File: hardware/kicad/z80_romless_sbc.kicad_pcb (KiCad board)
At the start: 2 copper layers, 160 x 135 mm, 69 parts, among them J1 REGULATED 5V INPUT, Q1 2N3904 MCP RESET, U1 Z84C0020PEC, U10 SN74LVC245AN bus-to-Pico, U2 AS6C1008-55PCN, U3 ATF22V10B/C, U4 SN74AHCT244N, U7 SN74LVC244AN, U8 MCP23S17-E/SP, U9 SN74AHCT245N Pico-to-bus

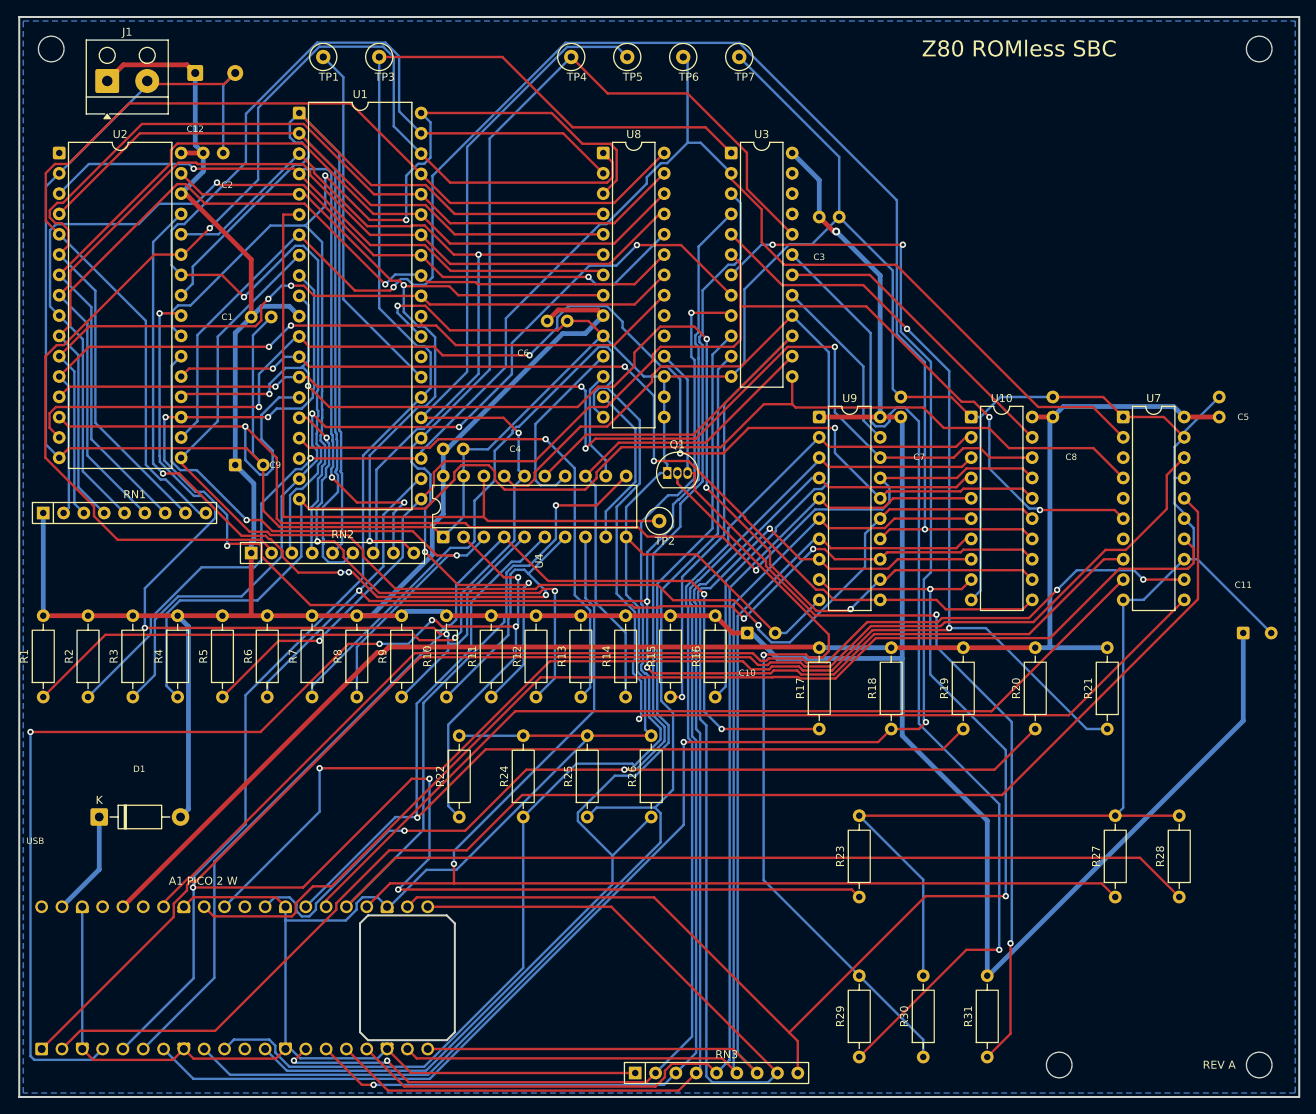
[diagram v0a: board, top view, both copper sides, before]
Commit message: feat: redesign PCB with four-layer stack
Reserve In1.Cu as a continuous ground plane, route signals on F.Cu/In2.Cu/B.Cu, and lock optimized via-free PICO_CLK and D4 paths for the 8 MHz qualification target. Regenerate and validate all KiCad and fabrication artifacts.

Co-authored-by: Copilot <223556219+Copilot@users.noreply.github.com>
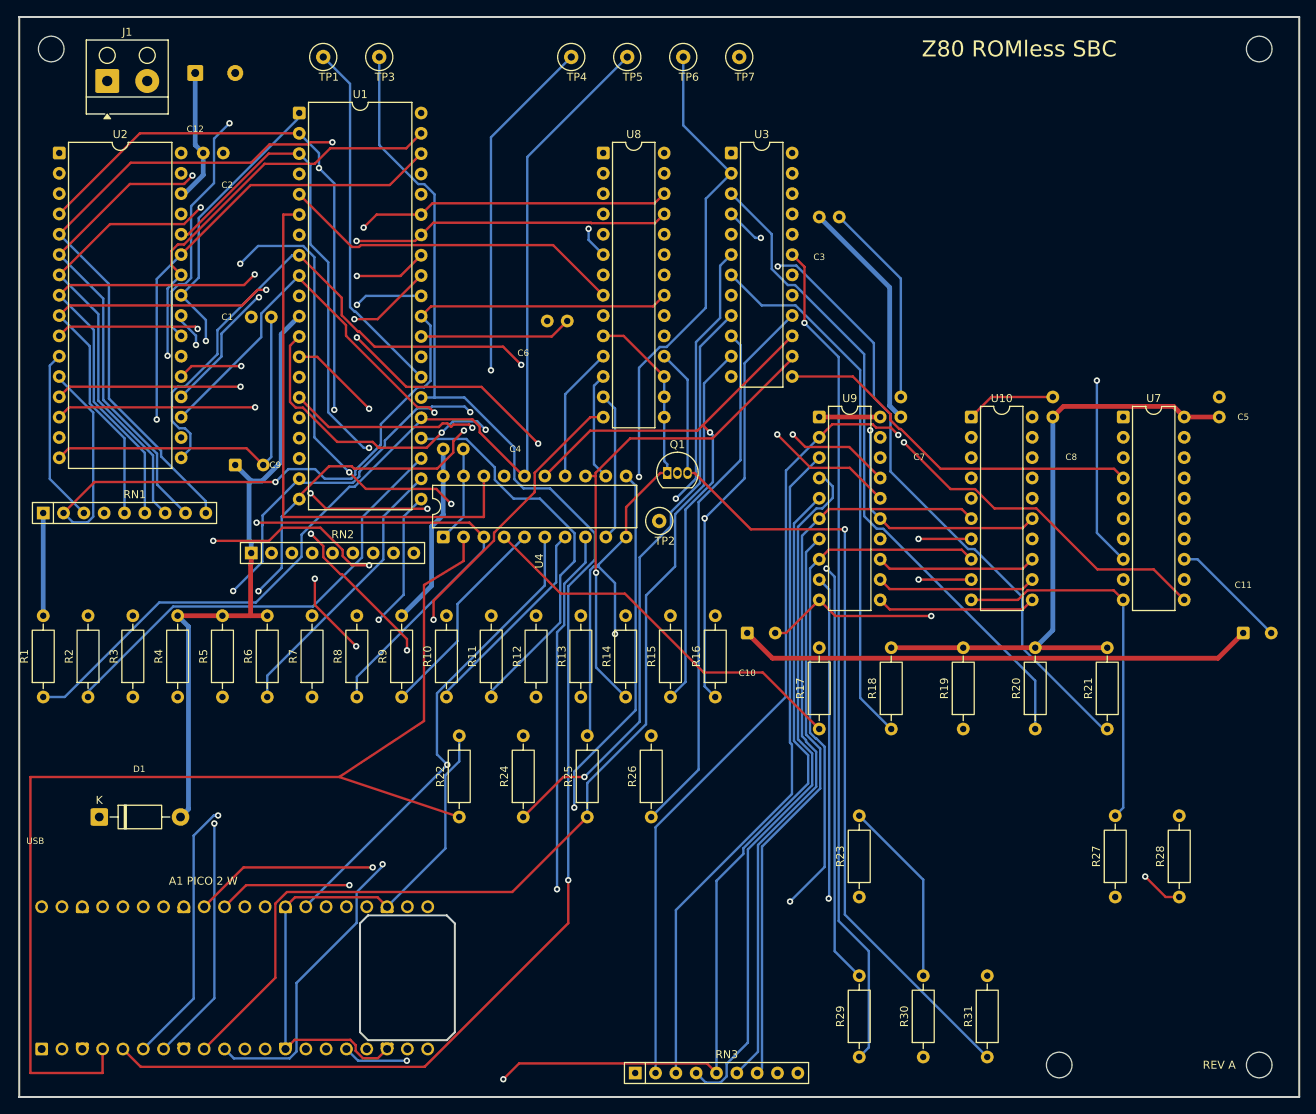
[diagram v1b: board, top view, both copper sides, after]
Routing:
- net MCP_SO: track 192.4 -> 138.8 mm, vias 1 -> 2
- net A8: track 154.9 -> 112.6 mm
- net A9: track 144.9 -> 109.0 mm
- net D1: track 164.9 -> 129.2 mm, vias 2 -> 3
- net PICO_D6: track 163.0 -> 132.2 mm
- net SRAM_OE_N: track 115.6 -> 87.1 mm
- net D5: track 166.1 -> 139.0 mm, vias 5 -> 1
- net WR_N: track 199.5 -> 173.1 mm, vias 3 -> 2
- net GND: track 795.3 -> 820.0 mm, vias 1 -> 2
- net RESET_N: track 300.8 -> 277.3 mm, vias 3 -> 1
- net SRAM_CE_PRE_N: track 102.2 -> 80.0 mm, vias 0 -> 1
- net PICO_SPI_MOSI: track 181.1 -> 159.0 mm, vias 1 -> 2
- net BUSREQ_N: track 159.5 -> 137.6 mm, vias 2 -> 0
- net MCP_RESET_DRIVE: track 126.6 -> 104.8 mm
- net PICO_D7: track 157.1 -> 135.6 mm
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- added copper zone on In1.Cu, net GND
- removed copper zone on B.Cu, net GND
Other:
- copper layers 2 -> 4

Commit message: feat: consolidate control pull-ups
Replace sixteen discrete 10k control pull-ups with two functionally grouped bussed SIP networks, reroute the four-layer board, and regenerate validated documentation and fabrication outputs.

Co-authored-by: Copilot <223556219+Copilot@users.noreply.github.com>
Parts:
- removed R1, R10, R11, R12, R13, R14, R15, R16, R2, R3, R4, R5, R6, R7, R8, R9: 10k, R_Axial_DIN0207_L6.3mm_D2.5mm_P10.16mm_Horizontal
- added RN4: 8x10k bussed, R_Array_SIP9, F.Cu at (30.0, 90.0)
- added RN5: 8x10k bussed, R_Array_SIP9, F.Cu at (72.0, 90.0)
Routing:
- net GND: track 820.0 -> 764.6 mm
- net BUSACK_N: track 216.2 -> 180.2 mm, vias 1 -> 2
- net PICO_BUSREQ_N: track 162.3 -> 134.5 mm, vias 1 -> 2
- net D5: track 139.0 -> 162.0 mm, vias 1 -> 2
- net NMI_N: track 63.2 -> 42.0 mm, vias 2 -> 0
- net BUSREQ_N: track 137.6 -> 116.4 mm, vias 0 -> 1
- net RD_N: track 174.0 -> 154.3 mm, vias 2 -> 1
- net +5V: track 504.0 -> 523.3 mm
- net INT_N: track 53.9 -> 38.2 mm, vias 2 -> 0
- net MCP_RESET_DRIVE: track 104.8 -> 118.4 mm, vias 1 -> 2
- net PICO_OE_N: track 204.4 -> 191.2 mm
- net RESET_N: track 277.3 -> 288.3 mm, vias 1 -> 3
- net PICO_SPI_MOSI: track 159.0 -> 169.9 mm, vias 2 -> 3
- net PICO_SPI_CS_N: track 126.0 -> 115.3 mm
- net A0: track 119.4 -> 109.1 mm
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
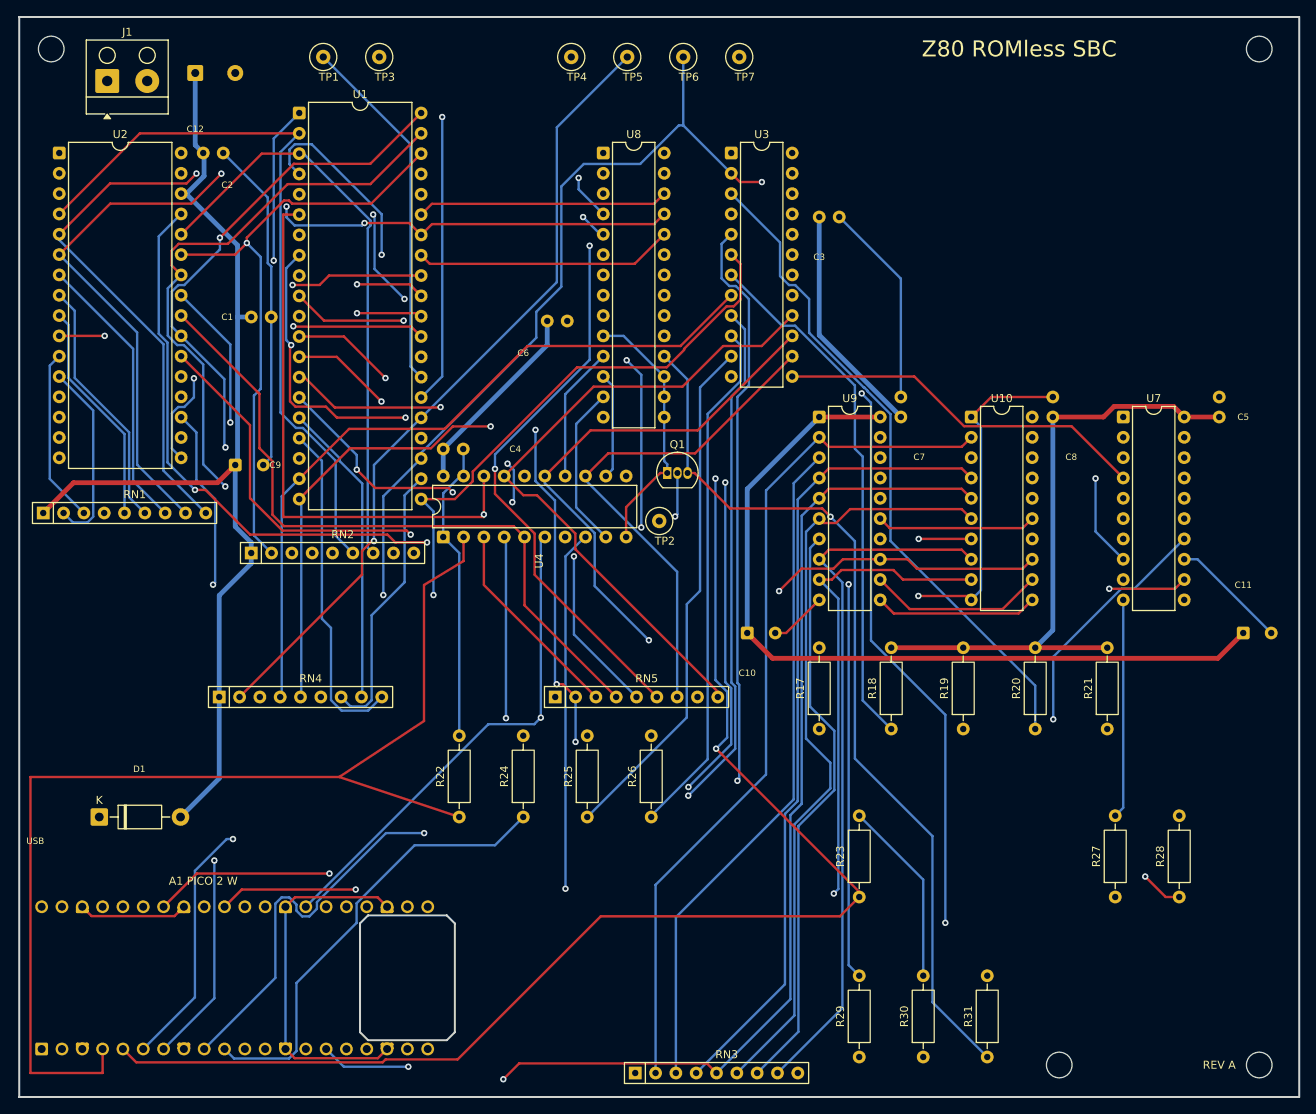
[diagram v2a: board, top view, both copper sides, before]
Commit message: Increase Z80 clock-buffer clearance
Split the spacing adjustment between U1 and U4 to preserve a compact clock path while increasing their socket pin-row clearance from 2.76 mm to 5.76 mm. Refresh the clean four-layer route and fabrication outputs.

Co-authored-by: Copilot <223556219+Copilot@users.noreply.github.com>
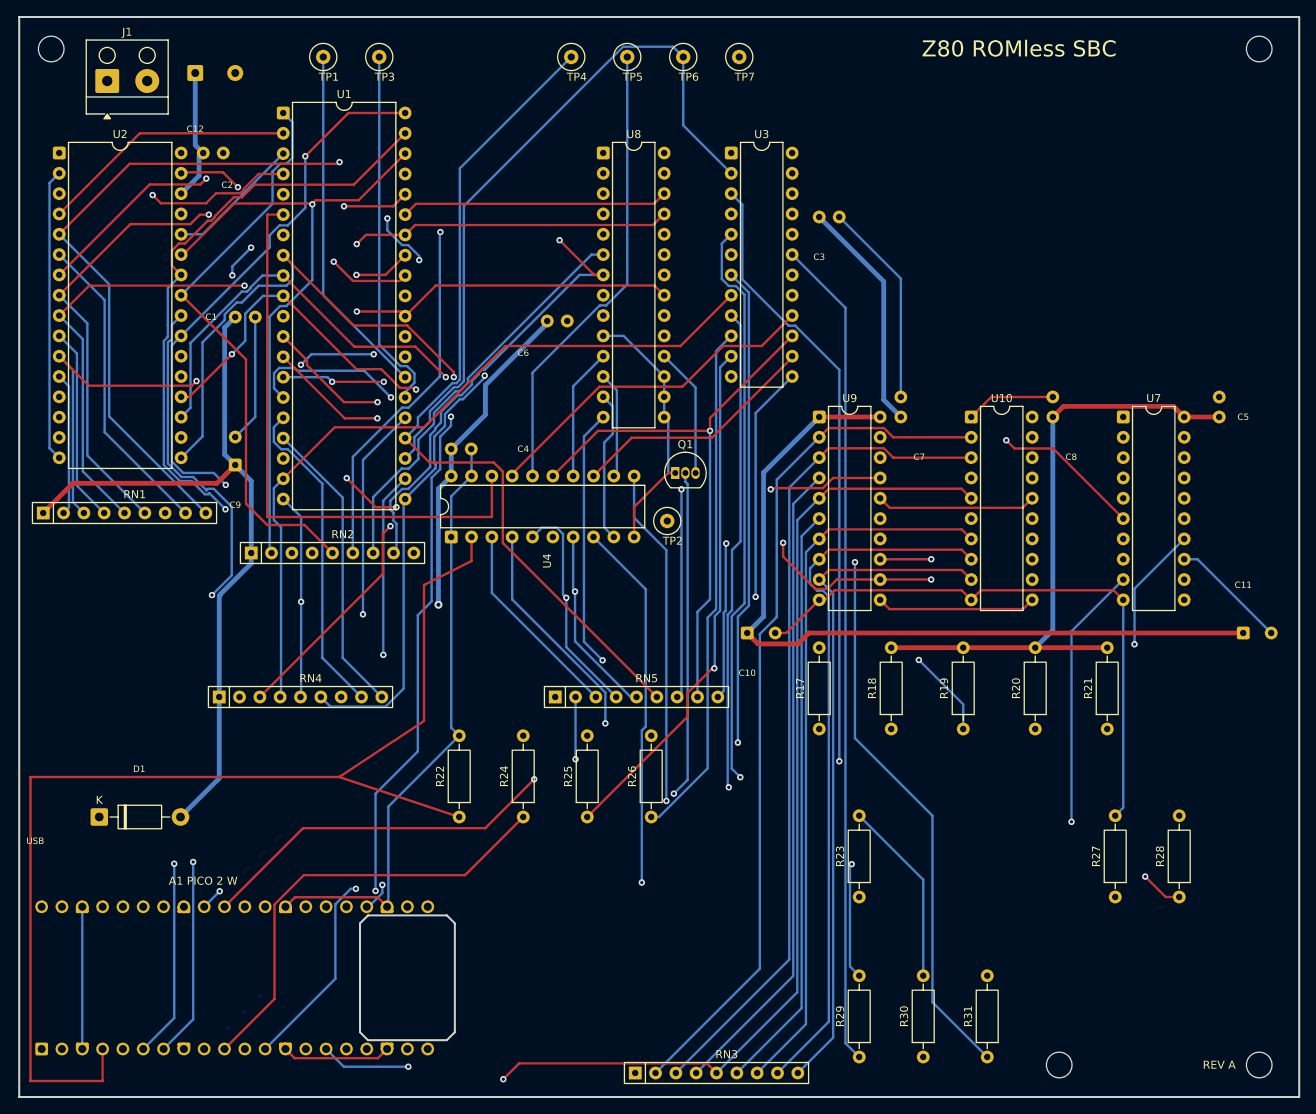
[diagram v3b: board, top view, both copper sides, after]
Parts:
- moved C1 2.00 mm to (32.0, 42.5)
- moved U1 2.00 mm to (38.0, 17.0)
- moved C4 1.00 mm to (59.0, 59.0)
- moved Q1 1.00 mm to (87.0, 62.0)
- moved TP2 1.00 mm to (86.0, 68.0)
- moved U4 1.00 mm to (59.0, 70.0)
- turned C9 to 90 degrees
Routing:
- net GND: track 764.6 -> 821.9 mm, vias 2 -> 0
- net +5V: track 523.3 -> 482.8 mm, vias 0 -> 1
- net PICO_SPI_CS_N: track 115.3 -> 154.6 mm
- net D5: track 162.0 -> 134.8 mm
- net SRAM_OE_N: track 87.0 -> 114.0 mm, vias 0 -> 2
- net SRAM_WE_N: track 112.7 -> 139.4 mm, vias 3 -> 1
- net D6: track 156.3 -> 134.9 mm, vias 3 -> 4
- net IORQ_N: track 140.5 -> 159.5 mm, vias 1 -> 2
- net RESET_N: track 288.3 -> 272.6 mm, vias 3 -> 2
- net MCP_RESET_DRIVE: track 118.4 -> 103.8 mm, vias 2 -> 0
- net A12: track 135.1 -> 122.5 mm
- net A5: track 117.1 -> 129.7 mm, vias 0 -> 1
- net PICO_SPI_MISO: track 123.0 -> 134.6 mm, vias 0 -> 1
- net PICO_SPI_MOSI: track 169.9 -> 158.5 mm, vias 3 -> 2
- net D3: track 153.5 -> 142.6 mm, vias 5 -> 1
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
